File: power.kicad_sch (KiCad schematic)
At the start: 1 part, among them U2 L7805

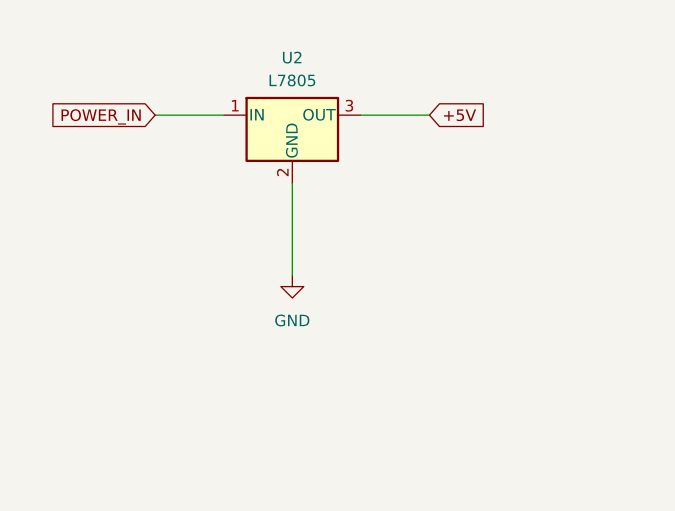
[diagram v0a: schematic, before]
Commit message: Added status LEDs.
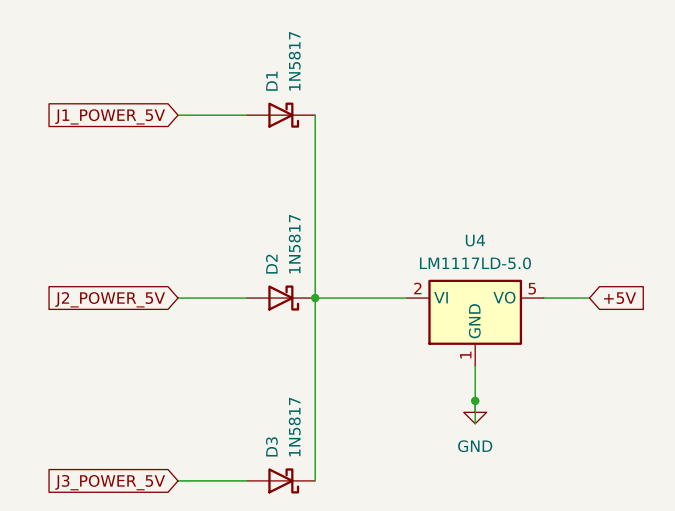
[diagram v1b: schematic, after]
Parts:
- removed U2: L7805, symbol Regulator_Linear:L7805
- added D1, D2, D3: 1N5817, Diode_SMD:D_1206_3216Metric, symbol Diode:1N5817
- added U4: LM1117LD-5.0, Package_SON:WSON-8-1EP_4x4mm_P0.8mm_EP2.2x3mm, symbol Regulator_Linear:LM1117LD-5.0
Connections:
- net +5V: now also U4.5 (VO), U4.6 (VO), U4.7 (VO), U4.9 (VO)
- net GND: now also U4.1 (GND)
- new net: D1.1 (K), D2.1 (K), D3.1 (K), U4.2 (VI), U4.3 (VI), U4.4 (VI)
- new net J1_POWER_5V: D1.2 (A)
- new net J2_POWER_5V: D2.2 (A)
- new net J3_POWER_5V: D3.2 (A)
